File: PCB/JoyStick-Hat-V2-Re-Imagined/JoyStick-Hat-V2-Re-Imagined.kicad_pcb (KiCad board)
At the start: 4 copper layers, 123 x 56 mm, 117 parts, among them J1 20021121-00010C4LF, J10 Conn_02x06_Odd_Even, J14 Conn_01x03_Pin, J15 Conn_01x03_Pin, J2 BU2032SM-JJ-GTR, J3 Conn_02x05_Odd_Even, J4 Conn_02x04_Odd_Even, J5 RJHSE-5381, J6 1757242, J7 Raspberry_Pi_2_3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

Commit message: Joystick Hat V2 Progress
Powersupply section laid out on V2 of JoyStick Hat PCB
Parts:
- C21: footprint AVR-KiCAD-Lib-Capacitors:CP_Elec_4x5.3 -> AVR-KiCAD-Lib-Capacitors:CAP_UUQ_6P3X5P4_NCH
- C22: footprint AVR-KiCAD-Lib-Capacitors:CP_Elec_4x5.3 -> AVR-KiCAD-Lib-Capacitors:CAP_UUQ_4X5P4_NCH
- moved H4 210.7 mm to (219.5, 106.5)
- moved H3 183.0 mm to (219.5, 57.5)
- moved J2 161.4 mm to (240.0, 135.8)
- moved H6 140.7 mm to (161.5, 106.5)
- moved C24 140.7 mm to (160.8, 99.8), turned to 90 degrees
- moved H2 133.4 mm to (161.5, 57.5)
- moved C23 133.0 mm to (155.5, 99.7)
- moved M3 130.0 mm to (200.1, 92.9)
- moved R20 130.0 mm to (200.2, 90.0)
- moved M2 101.9 mm to (181.4, 92.9)
- moved R21 101.9 mm to (181.5, 90.1)
- moved H5 92.8 mm to (103.5, 106.5)
- moved J15 91.2 mm to (111.0, 24.5)
- moved C17 78.9 mm to (98.2, 35.5)
- moved R39 78.9 mm to (97.9, 37.0)
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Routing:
- net /RPi_Interface/RPI_ST_UART_CTS: track 49.0 -> 0.00 mm, vias 2 -> 0
- net +5V: track 46.8 -> 5.28 mm, vias 9 -> 1
- net Net-(J7-GPIO23): track 38.6 -> 0.00 mm
- net Net-(J7-GPIO22): track 36.4 -> 0.00 mm
- net Net-(J7-GPIO24): track 30.7 -> 0.00 mm
- net /RPi_Interface/RPI_ST_UART_TX: track 30.1 -> 0.00 mm, vias 1 -> 0
- net /Power/5V_PG: track 45.7 -> 18.6 mm
- net /Power/3.3V_PG: track 46.8 -> 20.1 mm
- net /RPi_Interface/RPI_ST_UART_RX: track 25.8 -> 0.00 mm
- net Net-(J7-GPIO25): track 24.5 -> 0.00 mm
- net /RPi_Interface/RPI_ST_UART_RTS: track 24.4 -> 0.00 mm
- net /JoyStick Interface/ROTARY1_POLE3: track 33.3 -> 14.5 mm
- net /JoyStick Interface/ROTARY1_POLE1: track 31.9 -> 14.3 mm
- net /JoyStick Interface/ROTARY2_POLE3: track 29.3 -> 11.9 mm
- net /JoyStick Interface/ROTARY1_POLE2: track 32.5 -> 15.4 mm
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- added copper zone on In2.Cu, net +24V
- removed copper zone on In2.Cu, net +5V
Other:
- outline, holes or cut-outs redrawn

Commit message: V2
Lots of progress made on version two of JoyStick Hat but the RPi 5 is going to be elimintated and an additional RS485 port added.
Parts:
- removed J10: Conn_02x06_Odd_Even, Connector_PinHeader_2.54mm:PinHeader_2x06_P2.54mm_Horizontal
- removed J14, J15: Conn_01x03_Pin, Connector_PinHeader_2.54mm:PinHeader_1x03_P2.54mm_Vertical
- added J11: 0705430002, AVR-KiCAD-Lib-Connectors:Shrouded_Pin_Header_Straight_1x03_Pitch2.54mm, F.Cu at (183.5, 56.8)
- added J9: 0705430002, AVR-KiCAD-Lib-Connectors:Shrouded_Pin_Header_Straight_1x03_Pitch2.54mm, F.Cu at (169.7, 56.8)
- added M1: Raspberry_Pi_5_B, AVR-KiCAD-Lib-Modules:Raspberry_Pi_5, F.Cu at (122.5, 82.0)
- J3: value Conn_02x05_Odd_Even -> 0901301210; footprint Connector_PinHeader_2.54mm:PinHeader_2x05_P2.54mm_Vertical -> AVR-KiCAD-Lib-Connectors:CON_901301210_MOL
- J4, J8: value Conn_02x04_Odd_Even -> 0901301108; footprint Connector_PinHeader_2.54mm:PinHeader_2x04_P2.54mm_Vertical -> AVR-KiCAD-Lib-Connectors:CON_901301108_MOL
- SW1: value TL3301NF260QG -> PTS636 SM43 SMTR LFS; footprint AVR-KiCAD-Lib-Mech-Switches:TL3301NF260QG -> AVR-KiCAD-Lib-Mech-Switches:PTS636 SM43 SMTR LFS
- moved D2 119.6 mm to (147.5, 91.5), turned to 0 degrees
- moved D1 119.4 mm to (147.5, 93.0), turned to 0 degrees
- moved D7 119.3 mm to (147.5, 94.5), turned to 0 degrees
- moved D6 119.2 mm to (147.5, 96.0), turned to 0 degrees
- moved D14 119.1 mm to (147.5, 102.0), turned to 0 degrees
- moved D5 119.1 mm to (147.5, 97.5), turned to 0 degrees
- moved D3 119.1 mm to (147.5, 100.5), turned to 0 degrees
- moved D4 119.0 mm to (147.4, 99.0), turned to 0 degrees
- moved R9 115.3 mm to (144.5, 91.5), turned to 0 degrees
- moved R8 115.2 mm to (144.5, 93.0), turned to 0 degrees
- moved R16 115.0 mm to (144.5, 94.5), turned to 0 degrees
- moved R15 114.9 mm to (144.5, 96.0), turned to 0 degrees
- moved R10 114.9 mm to (144.5, 102.0), turned to 0 degrees
- moved R14 114.9 mm to (144.5, 97.5), turned to 0 degrees
- moved R12 114.8 mm to (144.5, 100.5), turned to 0 degrees
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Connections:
- J3 pad 3: /STM32F446RET6-MCU/LED_DRIVER_XLAT -> /STM32F446RET6-MCU/LED_DRIVER_SCLK
- J3 pad 4: /STM32F446RET6-MCU/LED_DRIVER_SCLK -> /STM32F446RET6-MCU/LED_DRIVER_XLAT
- J3 pad 5: /STM32F446RET6-MCU/LED_DRIVER_BLANK2 -> /STM32F446RET6-MCU/LED_DRIVER_MOSI
- J3 pad 6: /STM32F446RET6-MCU/LED_DRIVER_MOSI -> /STM32F446RET6-MCU/LED_DRIVER_BLANK2
- J3 pad 7: /STM32F446RET6-MCU/LED_DRIVER_BLANK -> /STM32F446RET6-MCU/LED_DRIVER_XLAT2
- J3 pad 8: /STM32F446RET6-MCU/LED_DRIVER_XLAT2 -> /STM32F446RET6-MCU/LED_DRIVER_BLANK
- J4 pad 2: /JoyStick Interface/BUTTON1 -> /JoyStick Interface/BUTTON4
- J4 pad 4: /JoyStick Interface/BUTTON2 -> /JoyStick Interface/BUTTON3
- J4 pad 6: /JoyStick Interface/BUTTON3 -> /JoyStick Interface/BUTTON2
- J4 pad 8: /JoyStick Interface/BUTTON4 -> /JoyStick Interface/BUTTON1
- J8 pad 1: /JoyStick Interface/ROTARY1_POLE1 -> GND
- J8 pad 2: GND -> /JoyStick Interface/ROTARY2_POLE1
- J8 pad 3: /JoyStick Interface/ROTARY1_POLE2 -> /JoyStick Interface/ROTARY1_POLE3
- J8 pad 4: /JoyStick Interface/ROTARY2_POLE3 -> /JoyStick Interface/ROTARY2_POLE2
- J8 pad 5: /JoyStick Interface/ROTARY1_POLE3 -> /JoyStick Interface/ROTARY1_POLE2
- J8 pad 6: /JoyStick Interface/ROTARY2_POLE2 -> /JoyStick Interface/ROTARY2_POLE3
- J8 pad 7: GND -> /JoyStick Interface/ROTARY1_POLE1
- J8 pad 8: /JoyStick Interface/ROTARY2_POLE1 -> GND
- SW1 pad 1: /STM32F446RET6-MCU/NRST -> GND
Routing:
- net /Power/3.3V_PG: track 20.1 -> 88.0 mm
- net /Power/5V_PG: track 18.6 -> 72.3 mm
- net +5V: track 5.28 -> 51.7 mm
- net /RS485 To Motor Controller Interface/RS485_TX_LED: track 46.2 -> 92.1 mm
- net /RS485 To Motor Controller Interface/RS485_RX_LED: track 45.5 -> 90.3 mm
- net Net-(J7-GPIO23): track 0.00 -> 35.3 mm
- net Net-(J7-GPIO22): track 0.00 -> 34.7 mm
- net Net-(J7-GPIO24): track 0.00 -> 32.8 mm
- net /RPi_Interface/RPI_ST_UART_TX: track 0.00 -> 32.8 mm, vias 0 -> 1
- net /STM32F446RET6-MCU/LED_DRIVER_XLAT: track 14.2 -> 45.2 mm
- net /RPi_Interface/RPI_ST_UART_RX: track 0.00 -> 30.7 mm, vias 0 -> 1
- net /RPi_Interface/RPI_ST_UART_RTS: track 0.00 -> 28.4 mm, vias 0 -> 1
- net /STM32F446RET6-MCU/LED_DRIVER_SCLK: track 12.3 -> 39.5 mm
- net Net-(J7-GPIO25): track 0.00 -> 26.0 mm
- net /STM32F446RET6-MCU/LED_DRIVER_BLANK2: track 16.6 -> 40.4 mm
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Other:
- board text added: "JoyStick-HID Rev 0.2a 2024"
- board text removed: "12V Rail"
- board text removed: "JoyStick-HID Rev 0.1a 2024"

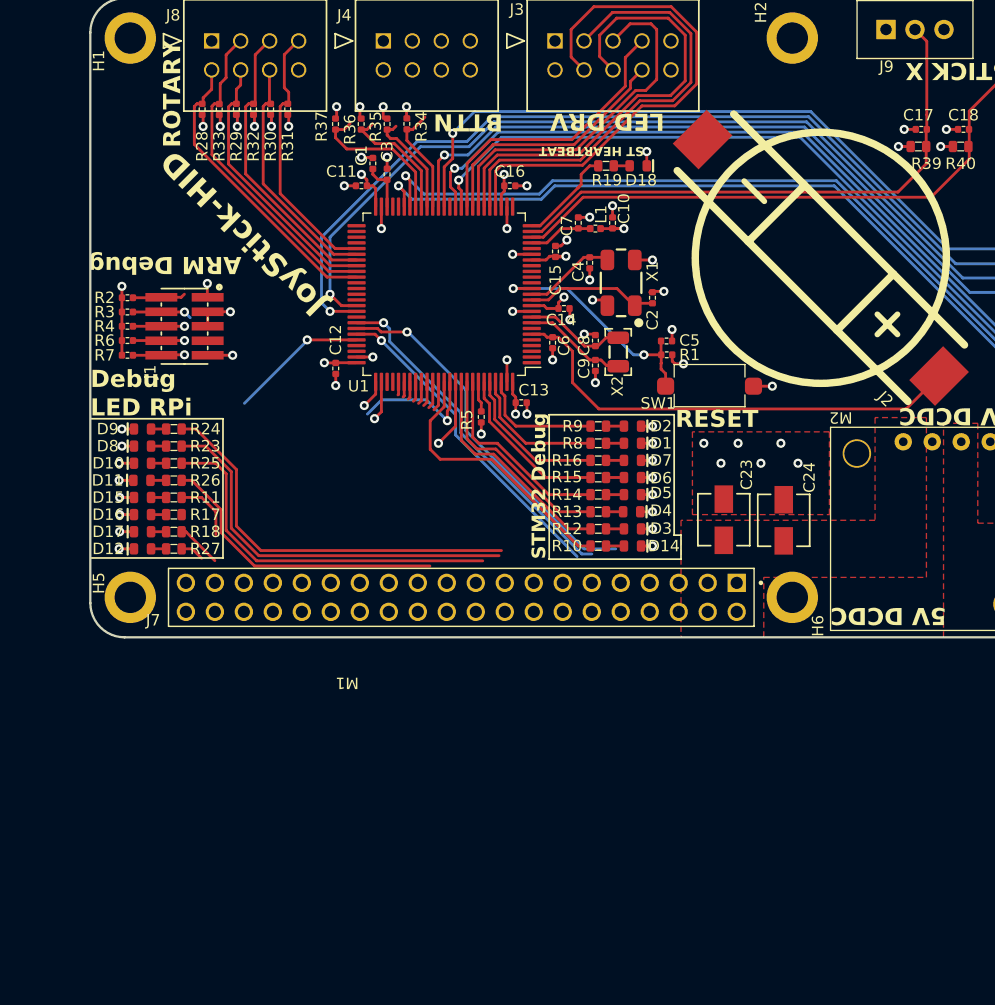
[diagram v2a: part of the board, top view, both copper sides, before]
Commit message: RPi Removed
Removed RPi from circuit added 20 pin JTAG schematic and PCB stil WIP
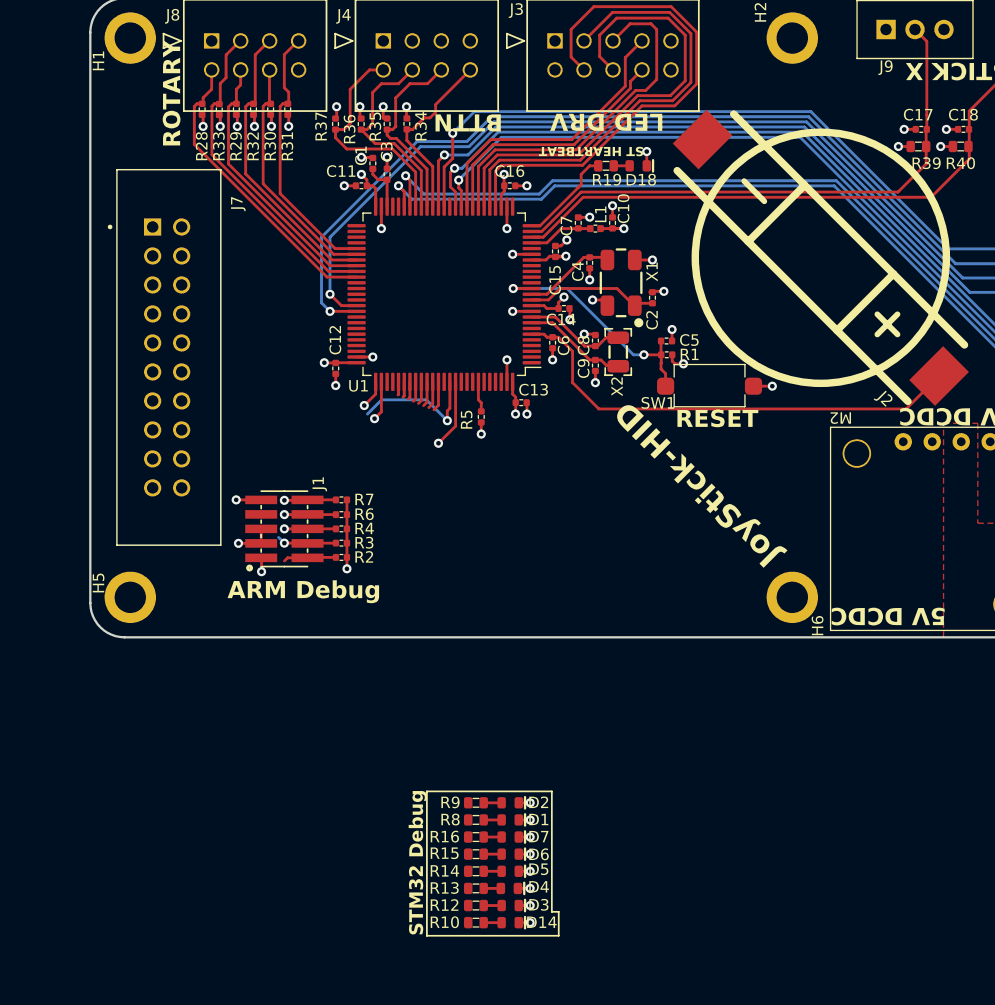
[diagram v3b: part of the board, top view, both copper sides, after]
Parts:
- removed C23, C24: UCM1C470MCL1GS, AVR-KiCAD-Lib-Capacitors:UCM1C470MCL1GS
- removed D10, D11, D12, D15, D16, D17, D8, D9: LTST-C194KGKT, AVR-KiCAD-Lib-Diodes:LED0603
- removed M1: Raspberry_Pi_5_B, AVR-KiCAD-Lib-Modules:Raspberry_Pi_5
- removed R11, R17, R18, R23, R24, R25, R26, R27: RC0603FR-07470RL, AVR-KiCAD-Lib-Resistors:R0603
- J7: value Raspberry_Pi_2_3 -> SBH11-PBPC-D10-ST-BK; footprint AVR-KiCAD-Lib-Connectors:SULLINS_PPPC202LFBN-RC_RPi5 -> AVR-KiCAD-Lib-Connectors:SULLINS_SBH11-PBPC-D10-ST-BK
- moved D1 34.7 mm to (136.8, 126.0)
- moved D14 34.7 mm to (136.8, 135.0)
- moved D2 34.7 mm to (136.8, 124.5)
- moved D3 34.7 mm to (136.8, 133.5)
- moved D4 34.7 mm to (136.7, 132.0)
- moved D5 34.7 mm to (136.8, 130.5)
- moved D6 34.7 mm to (136.8, 129.0)
- moved D7 34.7 mm to (136.8, 127.5)
- moved R10 34.7 mm to (133.8, 135.0)
- moved R12 34.7 mm to (133.8, 133.5)
- moved R13 34.7 mm to (133.8, 132.0)
- moved R14 34.7 mm to (133.8, 130.5)
- moved R15 34.7 mm to (133.8, 129.0)
- moved R16 34.7 mm to (133.8, 127.5)
- moved R8 34.7 mm to (133.8, 126.0)
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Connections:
- J7 pad 1: unconnected-(J7-3V3-Pad1) -> +3.3V
- J7 pad 10: /RPi_Interface/RPI_ST_UART_RX -> GND
- J7 pad 11: /RPi_Interface/RPI_ST_UART_RTS -> /STM32F446RET6-MCU/NJTRST
- J7 pad 12: unconnected-(J7-GPIO18/PWM0-Pad12) -> GND
- J7 pad 13: unconnected-(J7-GPIO27-Pad13) -> /STM32F446RET6-MCU/NRST
- J7 pad 15: Net-(J7-GPIO22) -> /STM32F446RET6-MCU/DBG_DBRQ
- J7 pad 16: Net-(J7-GPIO23) -> GND
- J7 pad 17: unconnected-(J7-3V3-Pad17) -> /STM32F446RET6-MCU/DBG_DBDI
- J7 pad 18: Net-(J7-GPIO24) -> GND
- J7 pad 2: +5V -> GND
- J7 pad 3: unconnected-(J7-SDA/GPIO2-Pad3) -> /STM32F446RET6-MCU/SWCLK_TCK
- J7 pad 4: +5V -> GND
- J7 pad 5: unconnected-(J7-SCL/GPIO3-Pad5) -> /STM32F446RET6-MCU/SWDIO_TMS
- J7 pad 7: unconnected-(J7-GCLK0/GPIO4-Pad7) -> /STM32F446RET6-MCU/SWO_TDI
- J7 pad 8: /RPi_Interface/RPI_ST_UART_TX -> GND
- J7 pad 9: GND -> /STM32F446RET6-MCU/SWO_TDO
- R12 pad 1: Net-(U1-PB5) -> unconnected-(R12-Pad1)
- R13 pad 1: Net-(U1-PB6) -> unconnected-(R13-Pad1)
- R14 pad 1: Net-(U1-PB7) -> unconnected-(R14-Pad1)
- R15 pad 1: Net-(U1-PB8) -> unconnected-(R15-Pad1)
- R16 pad 1: Net-(U1-PB9) -> unconnected-(R16-Pad1)
- U1 pad 68: /RPi_Interface/RPI_ST_UART_RX -> unconnected-(U1-PA9-Pad68)
- U1 pad 69: /RPi_Interface/RPI_ST_UART_TX -> unconnected-(U1-PA10-Pad69)
- U1 pad 70: /RPi_Interface/RPI_ST_UART_RTS -> unconnected-(U1-PA11-Pad70)
- U1 pad 71: /RPi_Interface/RPI_ST_UART_CTS -> unconnected-(U1-PA12-Pad71)
- U1 pad 91: Net-(U1-PB5) -> /STM32F446RET6-MCU/DBG_DBRQ
- U1 pad 92: Net-(U1-PB6) -> /STM32F446RET6-MCU/DBG_DBDI
- U1 pad 93: Net-(U1-PB7) -> unconnected-(U1-PB7-Pad93)
- U1 pad 95: Net-(U1-PB8) -> unconnected-(U1-PB8-Pad95)
- U1 pad 96: Net-(U1-PB9) -> unconnected-(U1-PB9-Pad96)
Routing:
- net Net-(J7-GPIO23): track 35.3 -> 0.00 mm
- net Net-(J7-GPIO22): track 34.7 -> 0.00 mm
- net Net-(J7-GPIO24): track 32.8 -> 0.00 mm
- net /RPi_Interface/RPI_ST_UART_TX: track 32.8 -> 0.00 mm, vias 1 -> 0
- net /RPi_Interface/RPI_ST_UART_RX: track 30.7 -> 0.00 mm, vias 1 -> 0
- net /RPi_Interface/RPI_ST_UART_RTS: track 28.4 -> 0.00 mm, vias 1 -> 0
- net Net-(J7-GPIO25): track 26.0 -> 0.00 mm
- net Net-(U1-PD7): track 24.0 -> 0.00 mm
- net Net-(U1-PB5): track 19.7 -> 0.00 mm
- net Net-(U1-PB6): track 18.5 -> 0.00 mm
- net Net-(U1-PB7): track 17.5 -> 0.00 mm
- net Net-(U1-PB8): track 14.6 -> 0.00 mm
- net Net-(U1-PB9): track 13.4 -> 0.00 mm
- net /RPi_Interface/RPI_ST_UART_CTS: track 12.2 -> 0.00 mm, vias 1 -> 0
- net Net-(U1-PE0): track 12.2 -> 0.00 mm
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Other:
- board text removed: "Debug"
- board text removed: "LED RPi"

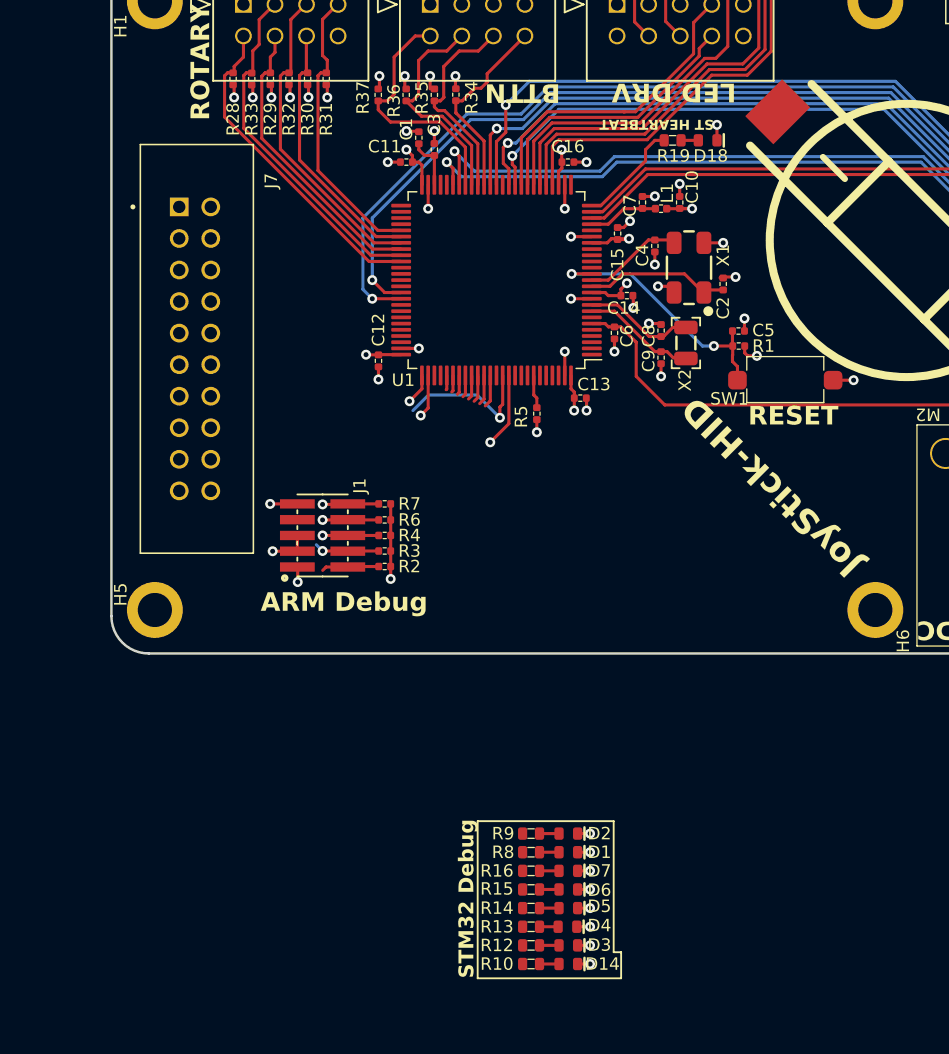
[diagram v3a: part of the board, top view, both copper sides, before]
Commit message: V2
V2 Schematic and Debug connector on PCB corrected
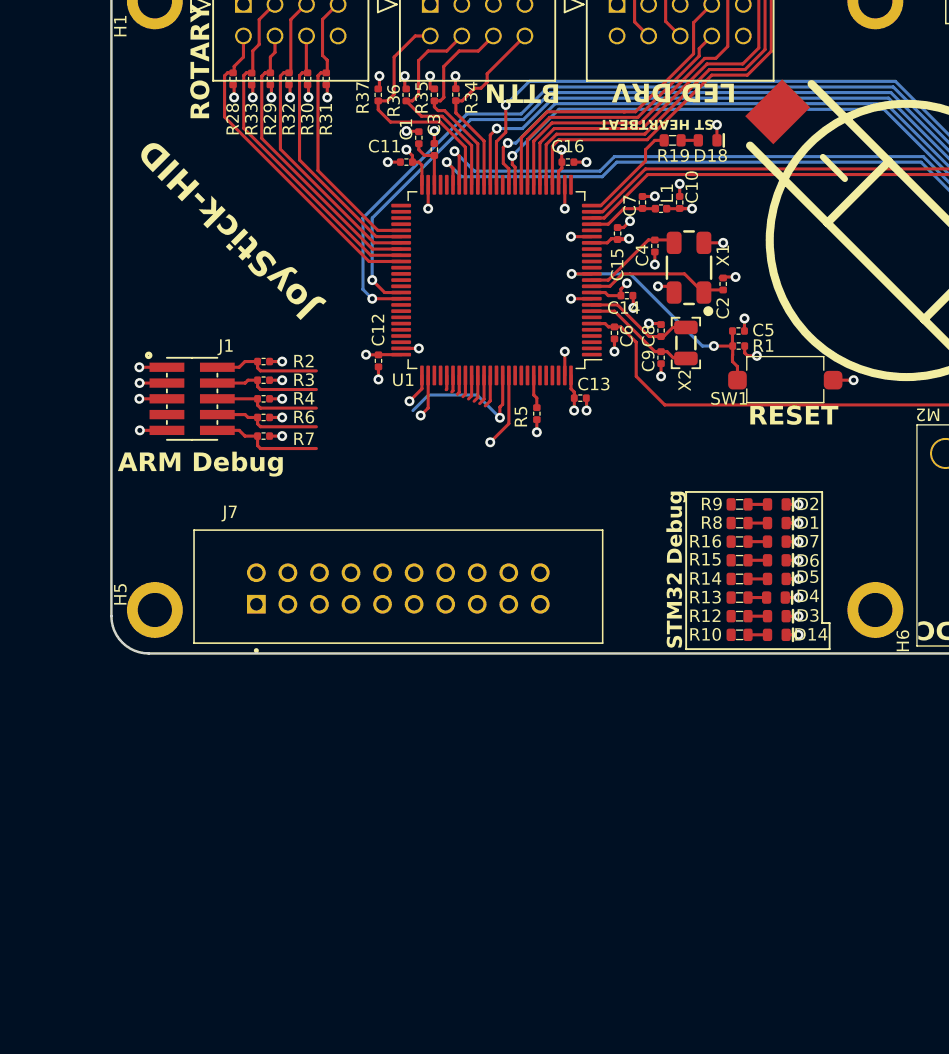
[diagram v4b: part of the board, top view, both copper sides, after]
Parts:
- moved D1 31.4 mm to (153.6, 99.5)
- moved D14 31.4 mm to (153.6, 108.5)
- moved D2 31.4 mm to (153.6, 98.0)
- moved D3 31.4 mm to (153.6, 107.0)
- moved D4 31.4 mm to (153.5, 105.5)
- moved D5 31.4 mm to (153.6, 104.0)
- moved D6 31.4 mm to (153.6, 102.5)
- moved D7 31.4 mm to (153.6, 101.0)
- moved R10 31.4 mm to (150.6, 108.5)
- moved R12 31.4 mm to (150.6, 107.0)
- moved R13 31.4 mm to (150.6, 105.5)
- moved R14 31.4 mm to (150.6, 104.0)
- moved R15 31.4 mm to (150.6, 102.5)
- moved R16 31.4 mm to (150.6, 101.0)
- moved R8 31.4 mm to (150.6, 99.5)
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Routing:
- net /STM32F446RET6-MCU/NJTRST: track 10.5 -> 15.0 mm, vias 2 -> 1
- net /STM32F446RET6-MCU/SWO_TDI: track 8.01 -> 12.2 mm, vias 2 -> 1
- net /STM32F446RET6-MCU/SWDIO_TMS: track 4.69 -> 8.77 mm
- net /STM32F446RET6-MCU/SWO_TDO: track 16.3 -> 20.4 mm, vias 2 -> 1
- net /STM32F446RET6-MCU/SWCLK_TCK: track 7.73 -> 11.2 mm, vias 2 -> 1
- net GND: track 66.2 -> 67.4 mm, vias 61 -> 62
- net +3.3V: vias 25 -> 29
